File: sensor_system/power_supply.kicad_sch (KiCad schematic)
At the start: 31 parts, among them J1 VBUS, J2 Solar_panels, Q1 SBC817, Q2 MJD45H11, SW1 SW_DPDT_x2, U1 MCP73833, U7 TPS63002

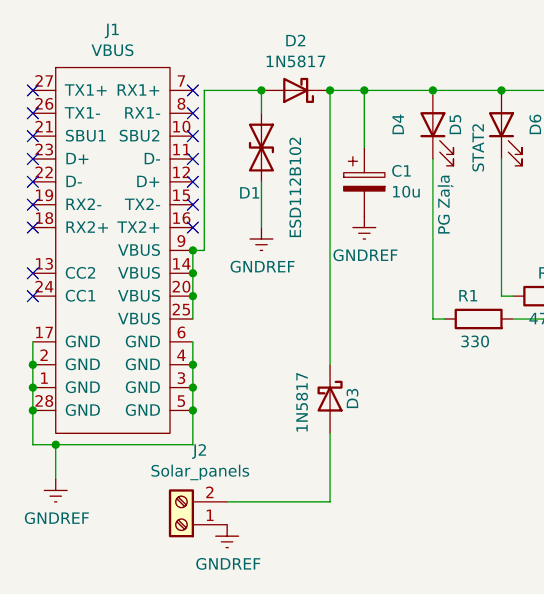
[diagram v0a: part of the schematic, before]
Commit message: Pievienoti footprint visām komponentēm
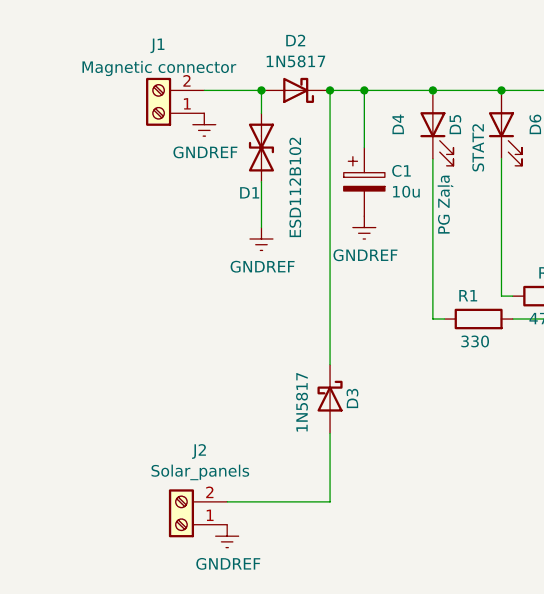
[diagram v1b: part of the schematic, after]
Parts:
- removed J1: VBUS, myLib:Type_C, symbol MyLibrary:Type_C
- added J1: Magnetic connector, symbol Connector:Screw_Terminal_01x02
- C2: footprint Capacitor_SMD:C_0805_2012Metric -> Capacitor_SMD:C_0603_1608Metric
- D2, D3: footprint myLib:DFLS240 -> Diode_SMD:D_SOD-123
- D4, D5: footprint LED_THT:LED_D5.0mm -> LED_SMD:LED_0805_2012Metric
- D6: footprint LED_THT:LED_D5.0mm -> LED_SMD:LED_0603_1608Metric
- D7: footprint Diode_SMD:D_SOD-123 -> Diode_SMD:D_SOD-123F
- L2: footprint (none) -> Inductor_SMD:L_Coilcraft_LPS4018
- Q1: footprint Connector_PinSocket_1.00mm:PinSocket_1x03_P1.00mm_Vertical_SMD_Pin1Left -> Package_TO_SOT_SMD:SOT-23-3
- Q2: footprint myLib:PNP -> Package_TO_SOT_SMD:TO-252-2
- R5: footprint Resistor_SMD:R_0603_1608Metric -> Resistor_SMD:R_0805_2012Metric
- U1: footprint myLib:MCP73833 -> MCP73833-BZI_UN:SOP50P490X110-10N
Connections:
- net GNDREF: now also J1.1 (Pin_1)
- net at D1.1 (A1), D2.2 (A): now also J1.2 (Pin_2)
- no-connect marks 17 -> 1

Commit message: Iespiedplate v1
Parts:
- J1: footprint (none) -> Magnetic connector:Magnetic connector
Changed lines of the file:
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@@
       (effects (font (size 1.27 1.27)))
     )
-    (property "Footprint" "" (at 31.75 27.94 0)
+    (property "Footprint" "Magnetic connector:Magnetic connector" (at 31.75 27.94 0)
       (effects (font (size 1.27 1.27)) hide)
     )

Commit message: Disaster in progress
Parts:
- added D6: ON/OFF, LED_SMD:LED_0603_1608Metric, symbol Device:LED
- added R3: 470, Resistor_SMD:R_0805_2012Metric, symbol Device:R
- J2: footprint TerminalBlock:TerminalBlock_bornier-2_P5.08mm -> TestPoint:TestPoint_2Pads_Pitch2.54mm_Drill0.8mm
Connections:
- net GNDREF: now also R3.1
- net at C2.1, Q2.2 (C), R8.1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: now also D6.2 (A)
- new net: D6.1 (K), R3.2
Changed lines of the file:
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@@
   (junction (at 78.74 25.4) (diameter 0) (color 0 0 0 0)
+  )
+  (junction (at 163.83 36.83) (diameter 0) (color 0 0 0 0)
   )
   (no_connect (at 134.62 41.91))
@@
     (stroke (width 0) (type default))
   )
-  (wire (pts (xy 168.91 36.83) (xy 162.56 36.83))
+  (wire (pts (xy 168.91 36.83) (xy 163.83 36.83))
     (stroke (width 0) (type default))
   )
@@
   )
   (wire (pts (xy 50.8 63.5) (xy 50.8 71.12))
+    (stroke (width 0) (type default))
+  )
+  (wire (pts (xy 163.83 36.83) (xy 162.56 36.83))
     (stroke (width 0) (type default))
   )
@@
       (effects (font (size 1.27 1.27)))
     )
-    (property "Footprint" "TerminalBlock:TerminalBlock_bornier-2_P5.08mm" (at 34.29 73.66 0)
+    (property "Footprint" "TestPoint:TestPoint_2Pads_Pitch2.54mm_Drill0.8mm" (at 34.29 73.66 0)
       (effects (font (size 1.27 1.27)) hide)
     )
@@
     )
   )
+  (symbol (lib_id "Device:LED") (at 163.83 40.64 90) (unit 1)
+    (in_bom yes) (on_board yes) (dnp no)
+    (property "Reference" "D6" (at 158.75 40.64 0)
+      (effects (font (size 1.27 1.27)))
+    )
+    (property "Value" "ON/OFF" (at 161.29 43.18 0)
+      (effects (font (size 1.27 1.27)))
+    )
+    (property "Footprint" "LED_SMD:LED_0603_1608Metric" (at 163.83 40.64 0)
+      (effects (font (size 1.27 1.27)) hide)
+    )
+    (property "Datasheet" "~" (at 163.83 40.64 0)
+      (effects (font (size 1.27 1.27)) hide)
+    )
+    (pin "1")
+    (pin "2")
+    (instances
+      (project "kursa projekts 2"
+        (path "/545a2faa-2381-4aac-bd87-ceae8eaeec05"
+          (reference "D6") (unit 1)
+        )
+      )
+      (project "sensor_system"
+        (path "/d745cb62-8f4d-408c-9af8-25e31ee1e0d0/89b6e76f-e734-47f0-98b1-101fd9e540da"
+          (reference "D10") (unit 1)
+        )
+      )
+    )
+  )
   (symbol (lib_id "power:GNDREF") (at 203.2 54.61 0) (unit 1)
     (in_bom yes) (on_board yes) (dnp no)
@@
     )
   )
+  (symbol (lib_id "Device:R") (at 163.83 48.26 180) (unit 1)
+    (in_bom yes) (on_board yes) (dnp no)
+    (property "Reference" "R3" (at 168.91 50.8 0)
+      (effects (font (size 1.27 1.27)) (justify left))
+    )
+    (property "Value" "470" (at 168.91 49.53 0)
+      (effects (font (size 1.27 1.27)) (justify left))
+    )
+    (property "Footprint" "Resistor_SMD:R_0805_2012Metric" (at 165.608 48.26 90)
+      (effects (font (size 1.27 1.27)) hide)
+    )
+    (property "Datasheet" "~" (at 163.83 48.26 0)
+      (effects (font (size 1.27 1.27)) hide)
+    )
+    (pin "1")
+    (pin "2")
+    (instances
+      (project "kursa projekts 2"
+        (path "/545a2faa-2381-4aac-bd87-ceae8eaeec05"
+          (reference "R3") (unit 1)
+        )
+      )
+      (project "sensor_system"
+        (path "/d745cb62-8f4d-408c-9af8-25e31ee1e0d0/89b6e76f-e734-47f0-98b1-101fd9e540da"
+          (reference "R14") (unit 1)
+        )
+      )
+    )
+  )
   (symbol (lib_id "Device:C_Small") (at 168.91 39.37 0) (unit 1)
     (in_bom yes) (on_board yes) (dnp no)
@@
         )
       )
+    )
+  )
+  (symbol (lib_id "power:GNDREF") (at 163.83 52.07 0) (unit 1)
+    (in_bom yes) (on_board yes) (dnp no)
+    (property "Reference" "#PWR07" (at 163.83 58.42 0)
+      (effects (font (size 1.27 1.27)) hide)
+    )
+    (property "Value" "GNDREF" (at 163.957 56.4642 0)
+      (effects (font (size 1.27 1.27)))
+    )
+    (property "Footprint" "" (at 163.83 52.07 0)
+      (effects (font (size 1.27 1.27)) hide)
+    )
+    (property "Datasheet" "" (at 163.83 52.07 0)
+      (effects (font (size 1.27 1.27)) hide)
+    )
+    (pin "1")
+    (instances
+      (project "kursa projekts 2"
+        (path "/545a2faa-2381-4aac-bd87-ceae8eaeec05"
+          (reference "#PWR07") (unit 1)
+        )
+      )
+      (project "sensor_system"
+        (path "/d745cb62-8f4d-408c-9af8-25e31ee1e0d0/89b6e76f-e734-47f0-98b1-101fd9e540da"
+          (reference "#PWR04") (unit 1)
+        )
+      )

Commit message: Board V1 with one mistake
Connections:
- net GNDREF renamed Earth

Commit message: Board fix 2.0
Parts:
- removed D1: ESD112B102, Diode_SMD:D_01005_0402Metric, symbol Device:D_TVS
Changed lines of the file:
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@@
   (junction (at 215.9 36.83) (diameter 0) (color 0 0 0 0)
-  )
-  (junction (at 43.18 25.4) (diameter 0) (color 0 0 0 0)
   )
   (junction (at 208.28 36.83) (diameter 0) (color 0 0 0 0)
@@
     (stroke (width 0) (type default))
   )
-  (wire (pts (xy 43.18 27.94) (xy 43.18 25.4))
-    (stroke (width 0) (type default))
-  )
   (wire (pts (xy 182.88 59.69) (xy 182.88 54.61))
     (stroke (width 0) (type default))
@@
   )
   (wire (pts (xy 69.85 25.4) (xy 62.23 25.4))
-    (stroke (width 0) (type default))
-  )
-  (wire (pts (xy 43.18 40.64) (xy 43.18 35.56))
     (stroke (width 0) (type default))
   )
@@
         (path "/d745cb62-8f4d-408c-9af8-25e31ee1e0d0/89b6e76f-e734-47f0-98b1-101fd9e540da"
           (reference "#PWR032") (unit 1)
-        )
-      )
-    )
-  )
-  (symbol (lib_id "power:GNDREF") (at 43.18 40.64 0) (unit 1)
-    (in_bom yes) (on_board yes) (dnp no)
-    (property "Reference" "#PWR03" (at 43.18 46.99 0)
-      (effects (font (size 1.27 1.27)) hide)
-    )
-    (property "Value" "GNDREF" (at 43.307 45.0342 0)
-      (effects (font (size 1.27 1.27)))
-    )
-    (property "Footprint" "" (at 43.18 40.64 0)
-      (effects (font (size 1.27 1.27)) hide)
-    )
-    (property "Datasheet" "" (at 43.18 40.64 0)
-      (effects (font (size 1.27 1.27)) hide)
-    )
-    (pin "1")
-    (instances
-      (project "kursa projekts 2"
-        (path "/545a2faa-2381-4aac-bd87-ceae8eaeec05"
-          (reference "#PWR03") (unit 1)
-        )
-      )
-      (project "sensor_system"
-        (path "/d745cb62-8f4d-408c-9af8-25e31ee1e0d0/89b6e76f-e734-47f0-98b1-101fd9e540da"
-          (reference "#PWR011") (unit 1)
         )
       )
@@
         )
       )
-    )
-  )
-  (symbol (lib_id "Device:D_TVS") (at 43.18 31.75 270) (unit 1)
-    (in_bom yes) (on_board yes) (dnp no)
-    (property "Reference" "D1" (at 40.64 36.83 90)
-      (effects (font (size 1.27 1.27)) (justify left))
-    )
-    (property "Value" "ESD112B102" (at 46.99 30.48 0)
-      (effects (font (size 1.27 1.27)) (justify left))
-    )
-    (property "Footprint" "Diode_SMD:D_01005_0402Metric" (at 43.18 31.75 0)
-      (effects (font (size 1.27 1.27)) hide)
-    )
-    (property "Datasheet" "~" (at 43.18 31.75 0)
-      (effects (font (size 1.27 1.27)) hide)
-    )
-    (pin "1")
-    (pin "2")
-    (instances
-      (project "kursa projekts 2"
-        (path "/545a2faa-2381-4aac-bd87-ceae8eaeec05"
-          (reference "D1") (unit 1)
-        )
-      )
-      (project "sensor_system"
-        (path "/d745cb62-8f4d-408c-9af8-25e31ee1e0d0/89b6e76f-e734-47f0-98b1-101fd9e540da"
-          (reference "D2") (unit 1)
-        )
-      )

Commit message: Gala versija
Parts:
- added TP1: TestPoint, Connector_PinHeader_1.00mm:PinHeader_1x01_P1.00mm_Vertical, symbol Connector:TestPoint
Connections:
- net at C2.1, D6.2 (A), Q2.2 (C)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: now also TP1.1
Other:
- moved on the sheet: C2, D6, L2, R3, R8, U7
